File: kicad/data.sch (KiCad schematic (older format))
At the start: 59 parts, among them J2 USB_B, J3 FTDI header, J4 PTT choice, J5 XCVR_CAT_TTL, J6 XCVR_PTT, U3 SN65220, U4 Si8663AB-B-IS1, U5 FT232RL, U6 SN74HCT32D, U7 VOR1121B6T

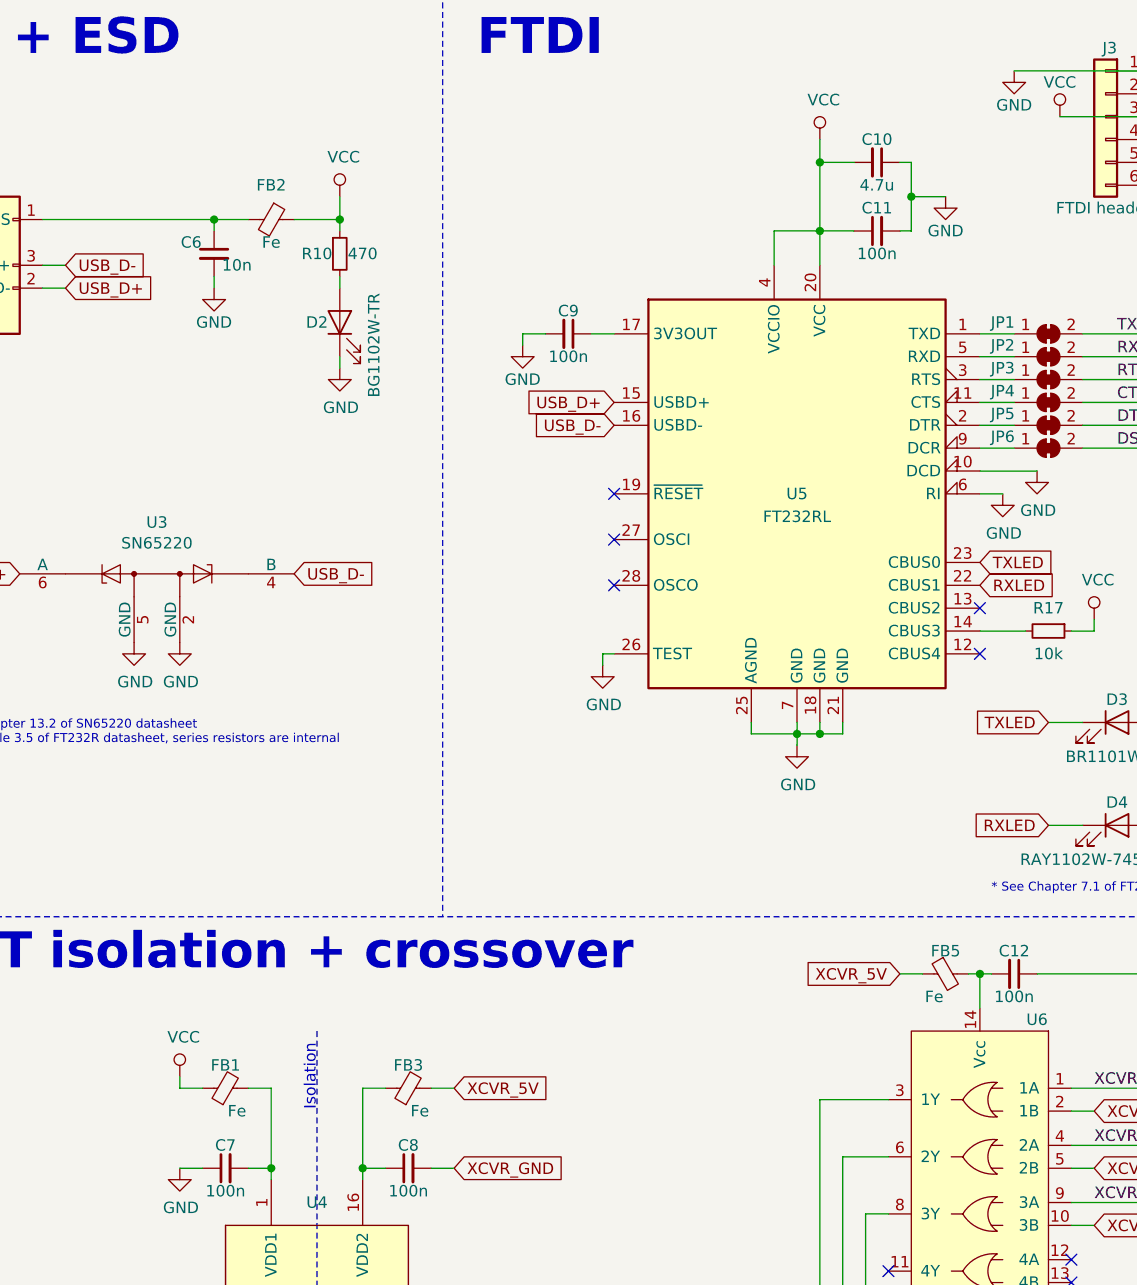
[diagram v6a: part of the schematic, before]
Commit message: Ferrite beads, hacking pads, audio fix
* Chose ferrite beads for IC Vcc (BLM31KN102SH1L)
* Change hacking pad thickness to 0.8mm
* Fixed potential oscillator when grounding audio- lines
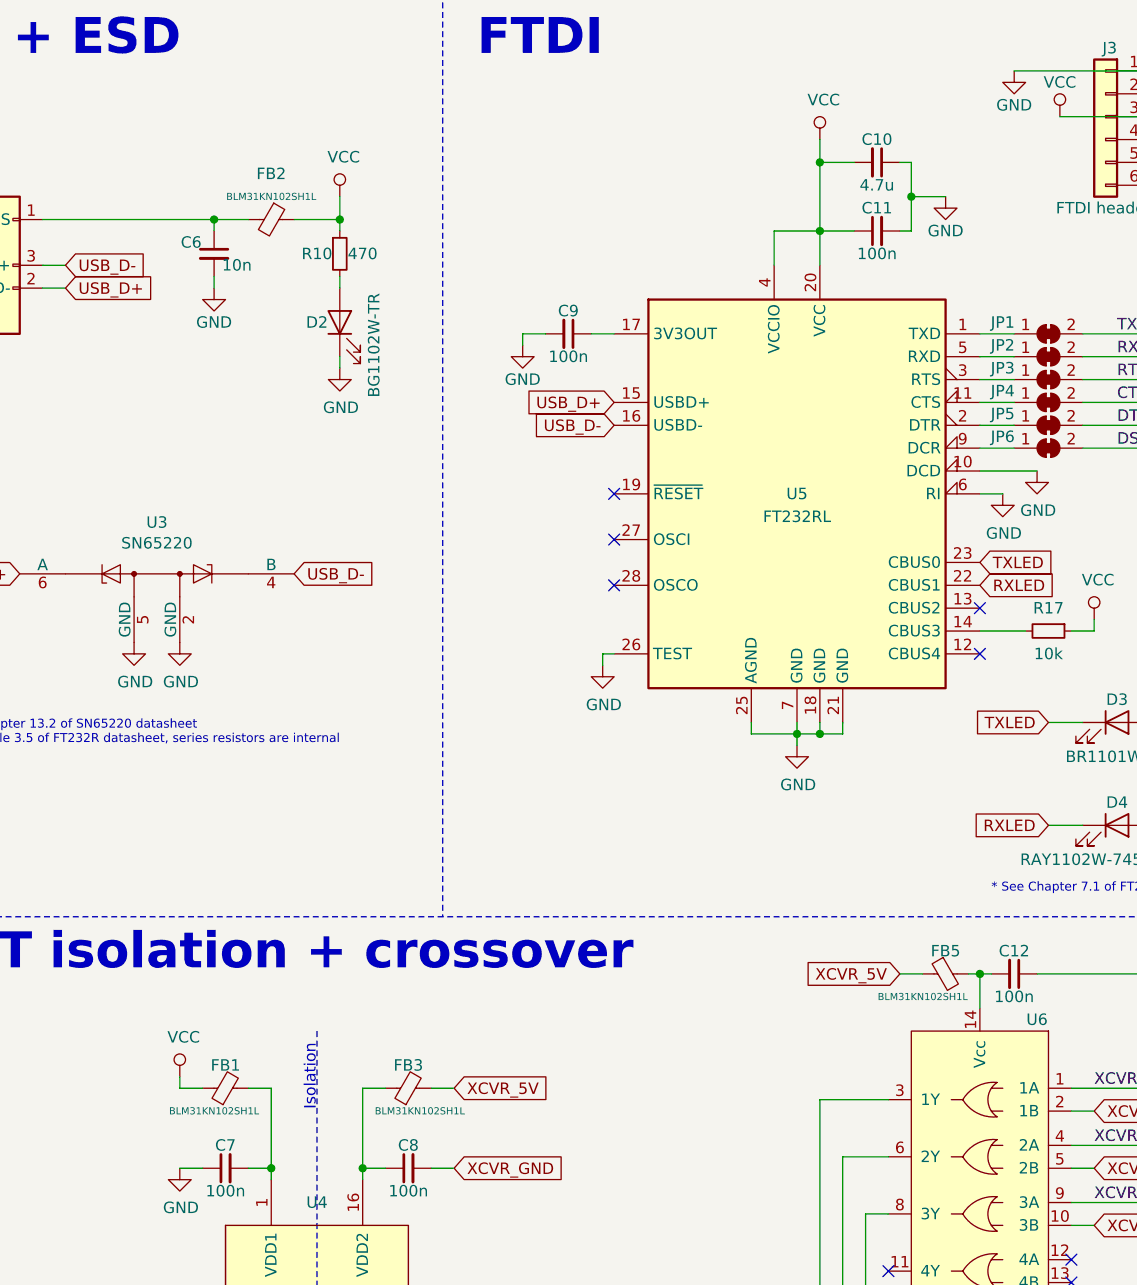
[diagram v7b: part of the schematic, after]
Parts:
- FB1, FB2, FB3, FB5: value Fe -> BLM31KN102SH1L
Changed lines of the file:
@@
 AR Path="/5F9D7A3C/5FD78EC7" Ref="FB?"  Part="1"
 AR Path="/5F9E7705/5FD78EC7" Ref="FB2"  Part="1"
-F 0 "FB2" V 2100 1450 50  0000 C CNN
-F 1 "Fe" V 2350 1450 50  0000 C CNN
+F 0 "FB2" V 2050 1450 50  0000 C CNN
+F 1 "BLM31KN102SH1L" V 2150 1450 31  0000 C CNN
 F 2 "Inductor_SMD:L_1206_3216Metric_Pad1.42x1.75mm_HandSolder" V 2180 1450 50  0001 C CNN
 F 3 "~" H 2250 1450 50  0001 C CNN
@@
 AR Path="/5F9E7705/5FB69FF0" Ref="FB1"  Part="1"
 F 0 "FB1" V 2150 5250 50  0000 C CNN
-F 1 "Fe" V 1950 5200 50  0000 C CNN
+F 1 "BLM31KN102SH1L" V 1950 5300 31  0000 C CNN
 F 2 "Inductor_SMD:L_1206_3216Metric_Pad1.42x1.75mm_HandSolder" V 1980 5250 50  0001 C CNN
 F 3 "~" H 2050 5250 50  0001 C CNN
@@
 AR Path="/5F9E7705/5FB84F16" Ref="FB3"  Part="1"
 F 0 "FB3" V 2950 5250 50  0000 C CNN
-F 1 "Fe" V 2750 5200 50  0000 C CNN
+F 1 "BLM31KN102SH1L" V 2750 5200 31  0000 C CNN
 F 2 "Inductor_SMD:L_1206_3216Metric_Pad1.42x1.75mm_HandSolder" V 2780 5250 50  0001 C CNN
 F 3 "~" H 2850 5250 50  0001 C CNN
@@
 AR Path="/5F9E7705/601885A8" Ref="FB5"  Part="1"
 F 0 "FB5" V 5100 4750 50  0000 C CNN
-F 1 "Fe" V 5300 4800 50  0000 C CNN
+F 1 "BLM31KN102SH1L" V 5300 4850 31  0000 C CNN
 F 2 "Inductor_SMD:L_1206_3216Metric_Pad1.42x1.75mm_HandSolder" V 5130 4750 50  0001 C CNN
 F 3 "~" H 5200 4750 50  0001 C CNN

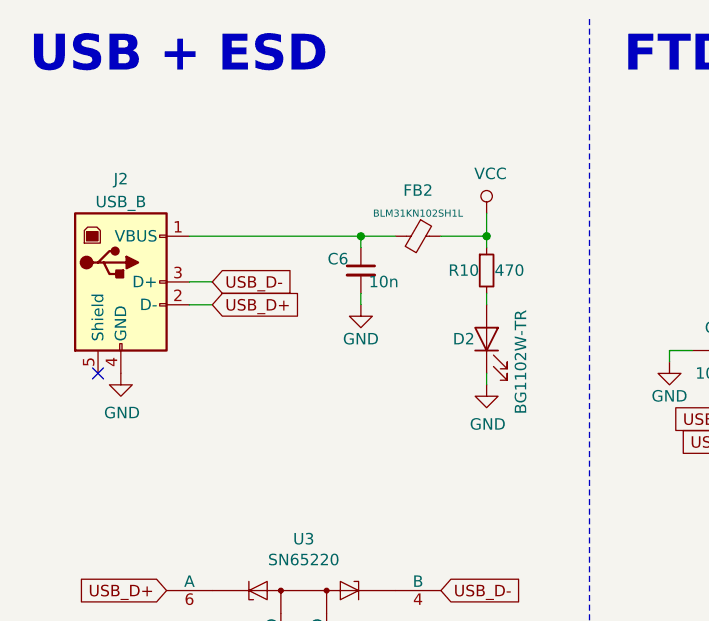
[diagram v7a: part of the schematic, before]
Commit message: Removed extra bypass cap from USB VBUS pin due to closeness to FTDI bypass cap; rerouted some traces
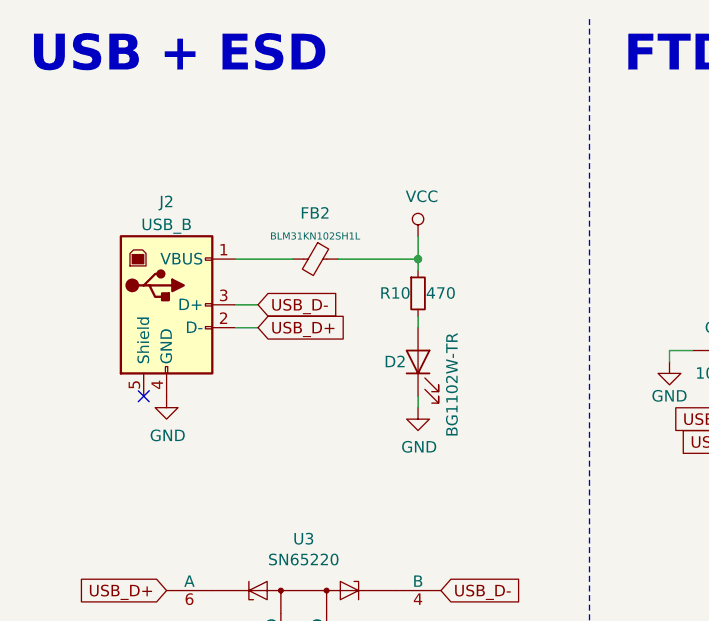
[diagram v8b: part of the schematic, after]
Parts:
- removed C6: 10n, Capacitor_SMD:C_1206_3216Metric_Pad1.42x1.75mm_HandSolder, symbol Device:C_Small
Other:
- moved on the sheet: D2, FB2, J2, R10
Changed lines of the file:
@@
 Comment4 ""
 $EndDescr
-Text GLabel 1350 1650 2    50   Input ~ 0
+Text GLabel 1550 1750 2    50   Input ~ 0
 USB_D-
 $Comp
 L power:GND #PWR?
 U 1 1 5FAB43A9
-P 950 2050
+P 1150 2150
 AR Path="/5FAB43A9" Ref="#PWR?"  Part="1"
 AR Path="/5F9E7705/5FAB43A9" Ref="#PWR03"  Part="1"
-F 0 "#PWR03" H 950 1800 50  0001 C CNN
-F 1 "GND" H 955 1877 50  0000 C CNN
-F 2 "" H 950 2050 50  0001 C CNN
-F 3 "" H 950 2050 50  0001 C CNN
-	1    950  2050
-	1    0    0    -1
-$EndComp
-Text GLabel 1350 1750 2    50   Input ~ 0
+F 0 "#PWR03" H 1150 1900 50  0001 C CNN
+F 1 "GND" H 1155 1977 50  0000 C CNN
+F 2 "" H 1150 2150 50  0001 C CNN
+F 3 "" H 1150 2150 50  0001 C CNN
+	1    1150 2150
+	1    0    0    -1
+$EndComp
+Text GLabel 1550 1850 2    50   Input ~ 0
 USB_D+
 $Comp
@@
 * See Chapter 7.1 of FT232R datasheet
 $Comp
-L Device:C_Small C?
-U 1 1 5FD78EA5
-P 2000 1600
-AR Path="/5FD78EA5" Ref="C?"  Part="1"
-AR Path="/5F9D7A3C/5FD78EA5" Ref="C?"  Part="1"
-AR Path="/5F9E7705/5FD78EA5" Ref="C6"  Part="1"
-F 0 "C6" H 1900 1650 50  0000 C CNN
-F 1 "10n" H 2100 1550 50  0000 C CNN
-F 2 "Capacitor_SMD:C_1206_3216Metric_Pad1.42x1.75mm_HandSolder" H 2000 1600 50  0001 C CNN
-F 3 "~" H 2000 1600 50  0001 C CNN
-	1    2000 1600
-	1    0    0    -1
-$EndComp
-$Comp
-L power:GND #PWR?
-U 1 1 5FD78EB1
-P 2000 1750
-AR Path="/5FD78EB1" Ref="#PWR?"  Part="1"
-AR Path="/5F9D7A3C/5FD78EB1" Ref="#PWR?"  Part="1"
-AR Path="/5F9E7705/5FD78EB1" Ref="#PWR09"  Part="1"
-F 0 "#PWR09" H 2000 1500 50  0001 C CNN
-F 1 "GND" H 2000 1600 50  0000 C CNN
-F 2 "" H 2000 1750 50  0001 C CNN
-F 3 "" H 2000 1750 50  0001 C CNN
-	1    2000 1750
-	1    0    0    -1
-$EndComp
-$Comp
 L power:VCC #PWR?
 U 1 1 5FD78EC1
-P 2550 1350
+P 2250 1450
 AR Path="/5FD78EC1" Ref="#PWR?"  Part="1"
 AR Path="/5F9D7A3C/5FD78EC1" Ref="#PWR?"  Part="1"
 AR Path="/5F9E7705/5FD78EC1" Ref="#PWR011"  Part="1"
-F 0 "#PWR011" H 2550 1200 50  0001 C CNN
-F 1 "VCC" H 2567 1523 50  0000 C CNN
-F 2 "" H 2550 1350 50  0001 C CNN
-F 3 "" H 2550 1350 50  0001 C CNN
-	1    2550 1350
+F 0 "#PWR011" H 2250 1300 50  0001 C CNN
+F 1 "VCC" H 2267 1623 50  0000 C CNN
+F 2 "" H 2250 1450 50  0001 C CNN
+F 3 "" H 2250 1450 50  0001 C CNN
+	1    2250 1450
 	1    0    0    -1
 $EndComp
@@
 L Device:Ferrite_Bead_Small FB?
 U 1 1 5FD78EC7
-P 2250 1450
+P 1800 1550
 AR Path="/5FD78EC7" Ref="FB?"  Part="1"
 AR Path="/5F9D7A3C/5FD78EC7" Ref="FB?"  Part="1"
 AR Path="/5F9E7705/5FD78EC7" Ref="FB2"  Part="1"
-F 0 "FB2" V 2050 1450 50  0000 C CNN
-F 1 "BLM31KN102SH1L" V 2150 1450 31  0000 C CNN
-F 2 "Inductor_SMD:L_1206_3216Metric_Pad1.42x1.75mm_HandSolder" V 2180 1450 50  0001 C CNN
-F 3 "~" H 2250 1450 50  0001 C CNN
-	1    2250 1450
+F 0 "FB2" V 1600 1550 50  0000 C CNN
+F 1 "BLM31KN102SH1L" V 1700 1550 31  0000 C CNN
+F 2 "Inductor_SMD:L_1206_3216Metric_Pad1.42x1.75mm_HandSolder" V 1730 1550 50  0001 C CNN
+F 3 "~" H 1800 1550 50  0001 C CNN
+	1    1800 1550
 	0    1    1    0
 $EndComp
@@
 Wire Wire Line
 	5650 4100 5800 4100
-Wire Wire Line
-	2000 1500 2000 1450
 Wire Notes Line
 	3000 500  3000 4500
@@
 Text Notes 10400 1000 0    39   Italic 0
 Screw terminal
-Wire Wire Line
-	2000 1450 2150 1450
-Connection ~ 2000 1450
-Wire Wire Line
-	2350 1450 2550 1450
 $Comp
 L Device:R_Small R?
 U 1 1 5FFE7E60
-P 2550 1600
+P 2250 1700
 AR Path="/5FFE7E60" Ref="R?"  Part="1"
 AR Path="/5F9D7A3C/5FFE7E60" Ref="R?"  Part="1"
 AR Path="/5F9E7705/5FFE7E60" Ref="R10"  Part="1"
-F 0 "R10" H 2450 1600 50  0000 C CNN
-F 1 "470" H 2650 1600 50  0000 C CNN
-F 2 "Resistor_SMD:R_1206_3216Metric_Pad1.42x1.75mm_HandSolder" H 2550 1600 50  0001 C CNN
-F 3 "~" H 2550 1600 50  0001 C CNN
-	1    2550 1600
+F 0 "R10" H 2150 1700 50  0000 C CNN
+F 1 "470" H 2350 1700 50  0000 C CNN
+F 2 "Resistor_SMD:R_1206_3216Metric_Pad1.42x1.75mm_HandSolder" H 2250 1700 50  0001 C CNN
+F 3 "~" H 2250 1700 50  0001 C CNN
+	1    2250 1700
 	1    0    0    -1
 $EndComp
@@
 L Device:LED D?
 U 1 1 5FFE90D2
-P 2550 1900
+P 2250 2000
 AR Path="/5FFE90D2" Ref="D?"  Part="1"
 AR Path="/5F9D7A3C/5FFE90D2" Ref="D?"  Part="1"
 AR Path="/5F9E7705/5FFE90D2" Ref="D2"  Part="1"
-F 0 "D2" V 2550 2000 50  0000 C CNN
-F 1 "BG1102W-TR" H 2450 1750 50  0000 C CNN
-F 2 "LED_SMD:LED_1206_3216Metric_Pad1.42x1.75mm_HandSolder" H 2550 1900 50  0001 C CNN
-F 3 "~" H 2550 1900 50  0001 C CNN
-	1    2550 1900
+F 0 "D2" V 2250 2100 50  0000 C CNN
+F 1 "BG1102W-TR" H 2150 1850 50  0000 C CNN
+F 2 "LED_SMD:LED_1206_3216Metric_Pad1.42x1.75mm_HandSolder" H 2250 2000 50  0001 C CNN
+F 3 "~" H 2250 2000 50  0001 C CNN
+	1    2250 2000
 	0    -1   -1   0
 $EndComp
@@
 L power:GND #PWR?
 U 1 1 5FFEA299
-P 2550 2100
+P 2250 2200
 AR Path="/5FFEA299" Ref="#PWR?"  Part="1"
 AR Path="/5F9D7A3C/5FFEA299" Ref="#PWR?"  Part="1"
 AR Path="/5F9E7705/5FFEA299" Ref="#PWR012"  Part="1"
-F 0 "#PWR012" H 2550 1850 50  0001 C CNN
-F 1 "GND" H 2555 1927 50  0000 C CNN
-F 2 "" H 2550 2100 50  0001 C CNN
-F 3 "" H 2550 2100 50  0001 C CNN
-	1    2550 2100
-	1    0    0    -1
-$EndComp
-Wire Wire Line
-	2000 1700 2000 1750
-Wire Wire Line
-	2550 1700 2550 1750
-Wire Wire Line
-	2550 2050 2550 2100
-Wire Wire Line
-	2550 1500 2550 1450
-Wire Wire Line
-	2550 1450 2550 1350
-Connection ~ 2550 1450
+F 0 "#PWR012" H 2250 1950 50  0001 C CNN
+F 1 "GND" H 2255 2027 50  0000 C CNN
+F 2 "" H 2250 2200 50  0001 C CNN
+F 3 "" H 2250 2200 50  0001 C CNN
+	1    2250 2200
+	1    0    0    -1
+$EndComp
+Wire Wire Line
+	2250 1800 2250 1850
+Wire Wire Line
+	2250 2150 2250 2200
+Wire Wire Line
+	2250 1600 2250 1550
+Wire Wire Line
+	2250 1550 2250 1450
+Connection ~ 2250 1550
 Text Notes 550  4750 0    157  ~ 31
 UART isolation + crossover
@@
 	1    0    0    -1
 $EndComp
-Wire Wire Line
-	4650 1100 4650 1200
 Connection ~ 4650 1200
 $Comp
@@
 L Connector:USB_B J2
 U 1 1 5F9FA669
-P 950 1650
-F 0 "J2" H 950 2100 50  0000 C CNN
-F 1 "USB_B" H 950 2000 50  0000 C CNN
-F 2 "Connector_USB:USB_B_OST_USB-B1HSxx_Horizontal" H 1100 1600 50  0001 C CNN
-F 3 " ~" H 1100 1600 50  0001 C CNN
-	1    950  1650
-	1    0    0    -1
-$EndComp
-Wire Wire Line
-	1250 1650 1350 1650
-Wire Wire Line
-	1250 1750 1350 1750
-Wire Wire Line
-	1250 1450 2000 1450
-NoConn ~ 850  2050
+P 1150 1750
+F 0 "J2" H 1150 2200 50  0000 C CNN
+F 1 "USB_B" H 1150 2100 50  0000 C CNN
+F 2 "Connector_USB:USB_B_OST_USB-B1HSxx_Horizontal" H 1300 1700 50  0001 C CNN
+F 3 " ~" H 1300 1700 50  0001 C CNN
+	1    1150 1750
+	1    0    0    -1
+$EndComp
+Wire Wire Line
+	1450 1750 1550 1750
+Wire Wire Line
+	1450 1850 1550 1850
+NoConn ~ 1050 2150
 Text GLabel 10350 1400 3    50   Input ~ 0
 XCVR_PTT-
@@
 Wire Wire Line
 	6750 5250 7000 5250
+Wire Wire Line
+	4650 1100 4650 1200
+Wire Wire Line
+	1450 1550 1700 1550
+Wire Wire Line
+	1900 1550 2250 1550
 Wire Bus Line
 	7700 1200 7700 1450
